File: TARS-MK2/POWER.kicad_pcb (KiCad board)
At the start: 2 copper layers, 69.9 x 162.4 mm, 20 parts, among them J701 XT60, J702 XT60, J703 SL_BATT1, J704 SL_BATT2, J705 TM_BATT1, J706 XT60, U701 D36V28F3, U702 D24V50F5, U703 LM7809_TO220, U704 D36V50F6, U705 D36V50F6, U706 D36V50F6, U707 D36V50F6

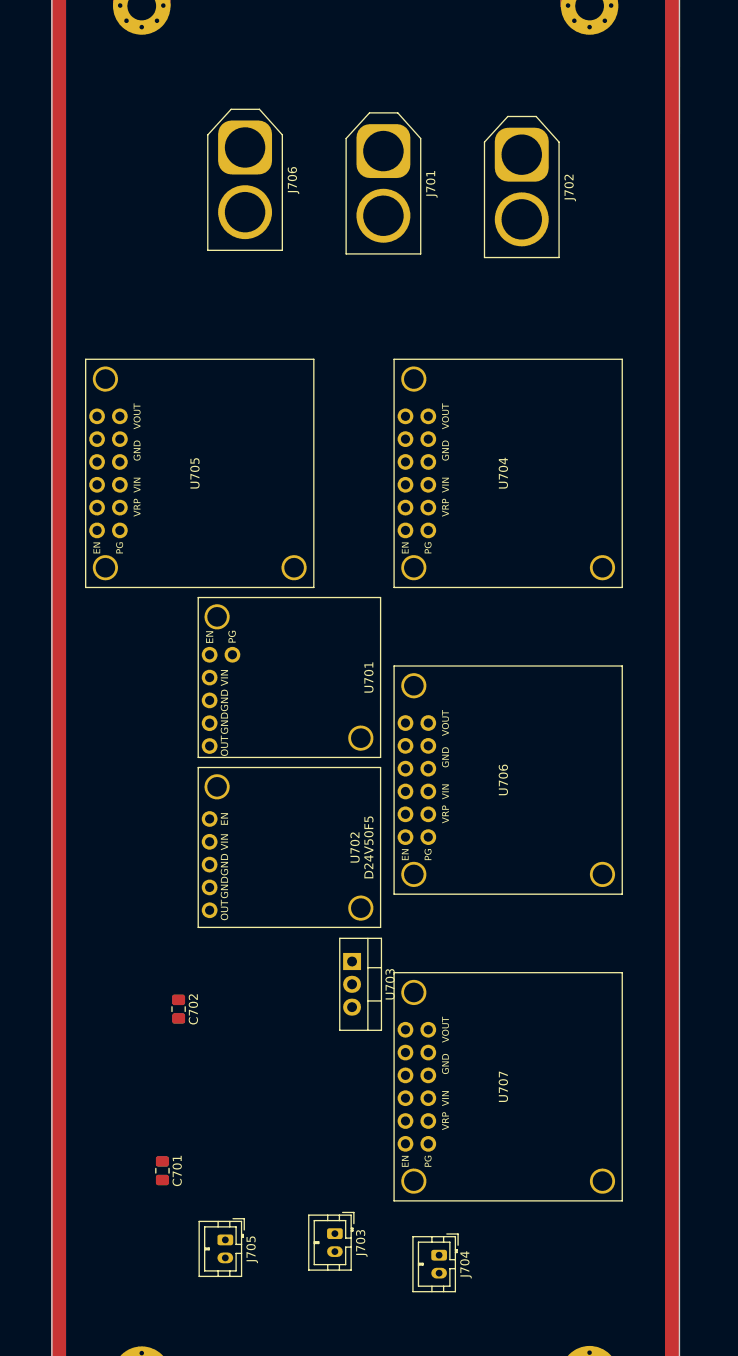
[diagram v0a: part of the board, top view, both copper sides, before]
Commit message: organized power board and added routes
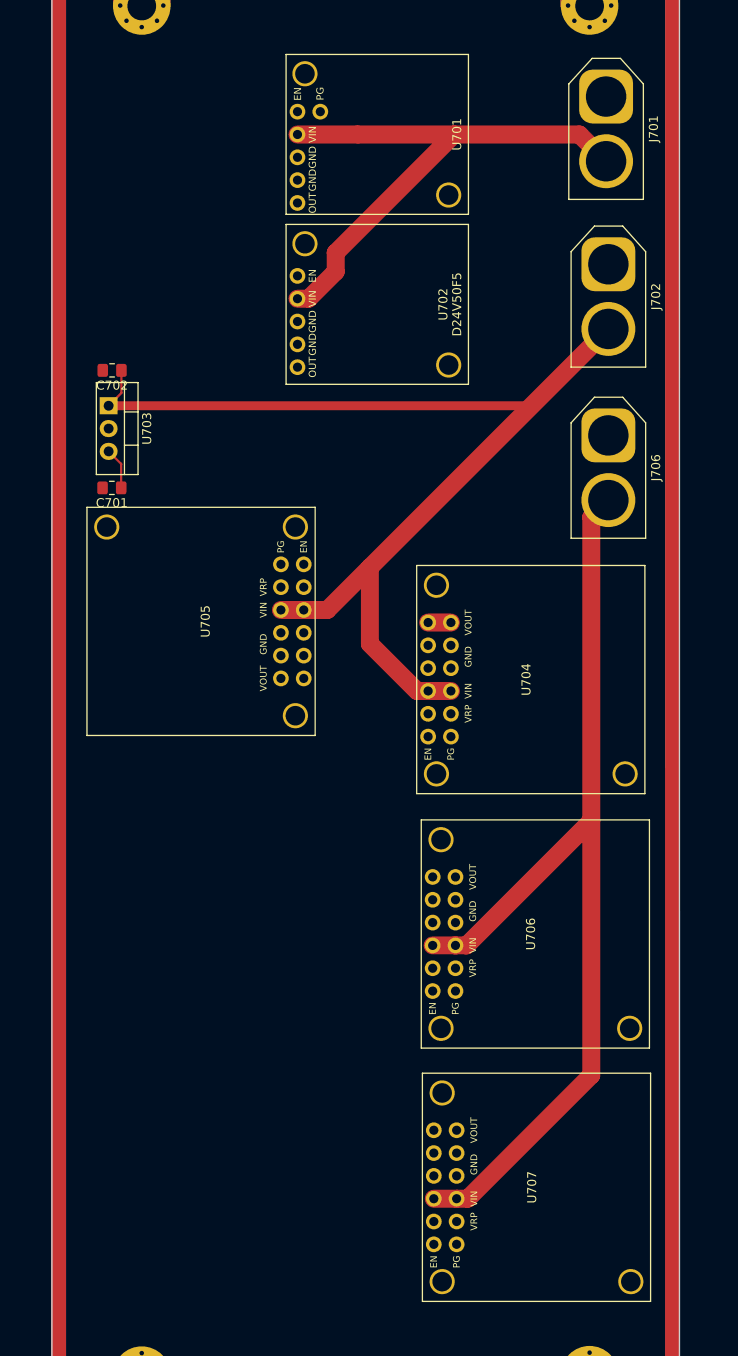
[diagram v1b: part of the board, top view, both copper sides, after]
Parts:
- removed J703: SL_BATT1, Connector_JST:JST_PH_B2B-PH-K_1x02_P2.00mm_Vertical
- removed J704: SL_BATT2, Connector_JST:JST_PH_B2B-PH-K_1x02_P2.00mm_Vertical
- removed J705: TM_BATT1, Connector_JST:JST_PH_B2B-PH-K_1x02_P2.00mm_Vertical
- moved C701 76.2 mm to (188.6, 118.5), turned to 180 degrees
- moved C702 71.5 mm to (188.6, 105.4), turned to 180 degrees
- moved U703 67.5 mm to (188.2, 109.3)
- moved U701 61.2 mm to (228.3, 79.1)
- moved U702 61.2 mm to (228.3, 98.1)
- moved J706 51.6 mm to (243.8, 112.6)
- moved U705 49.1 mm to (211.2, 146.1), turned to 90 degrees
- moved J701 25.5 mm to (243.6, 74.9)
- moved U704 23.1 mm to (222.5, 127.1)
- moved U706 17.4 mm to (223.0, 155.4)
- moved J702 15.5 mm to (243.8, 93.6)
- moved U707 11.6 mm to (223.1, 183.6)
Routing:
- net Net-(C702-Pad1): track 0.00 -> 133.3 mm
- net Net-(J706-Pad2): track 0.00 -> 111.4 mm
- net Net-(J701-Pad2): track 0.00 -> 61.8 mm
- net 9V_PT_SUPPLY: track 0.00 -> 4.64 mm
- net 6V_HYBRID_SERVO0: track 0.00 -> 2.54 mm

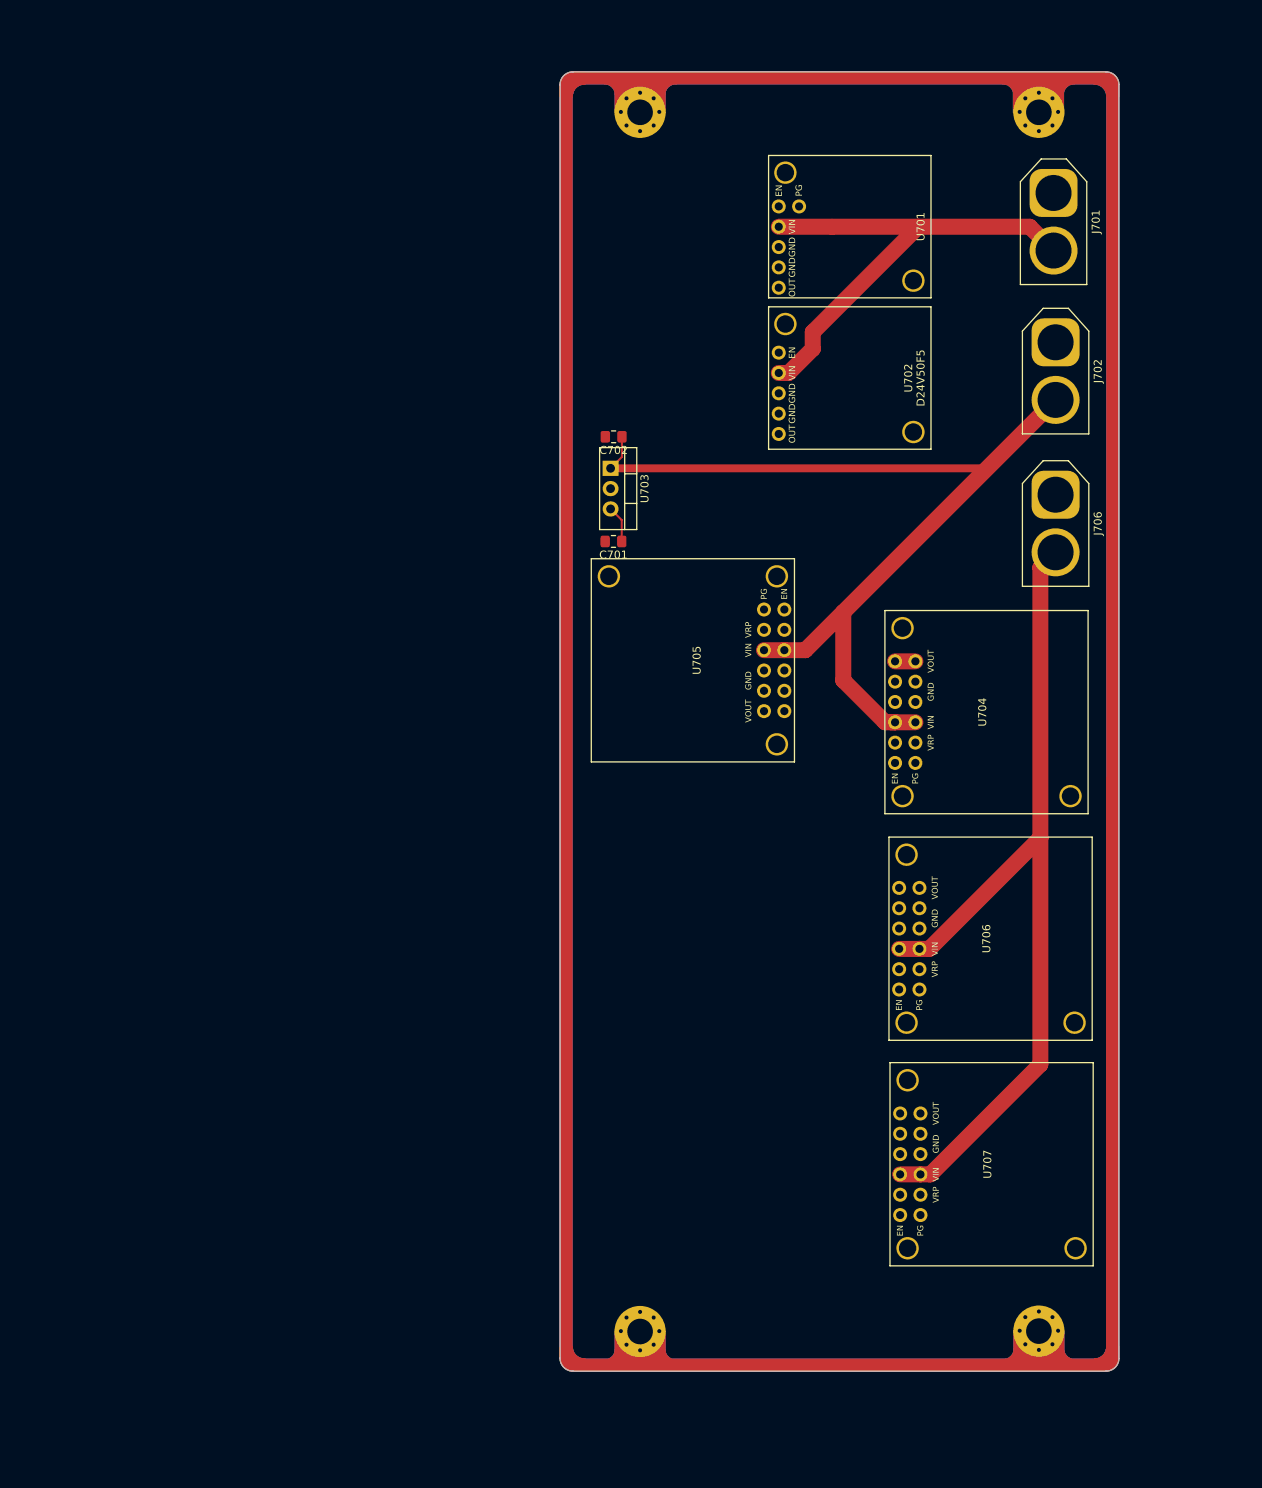
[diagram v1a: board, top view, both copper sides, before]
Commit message: Power Board molex connectors
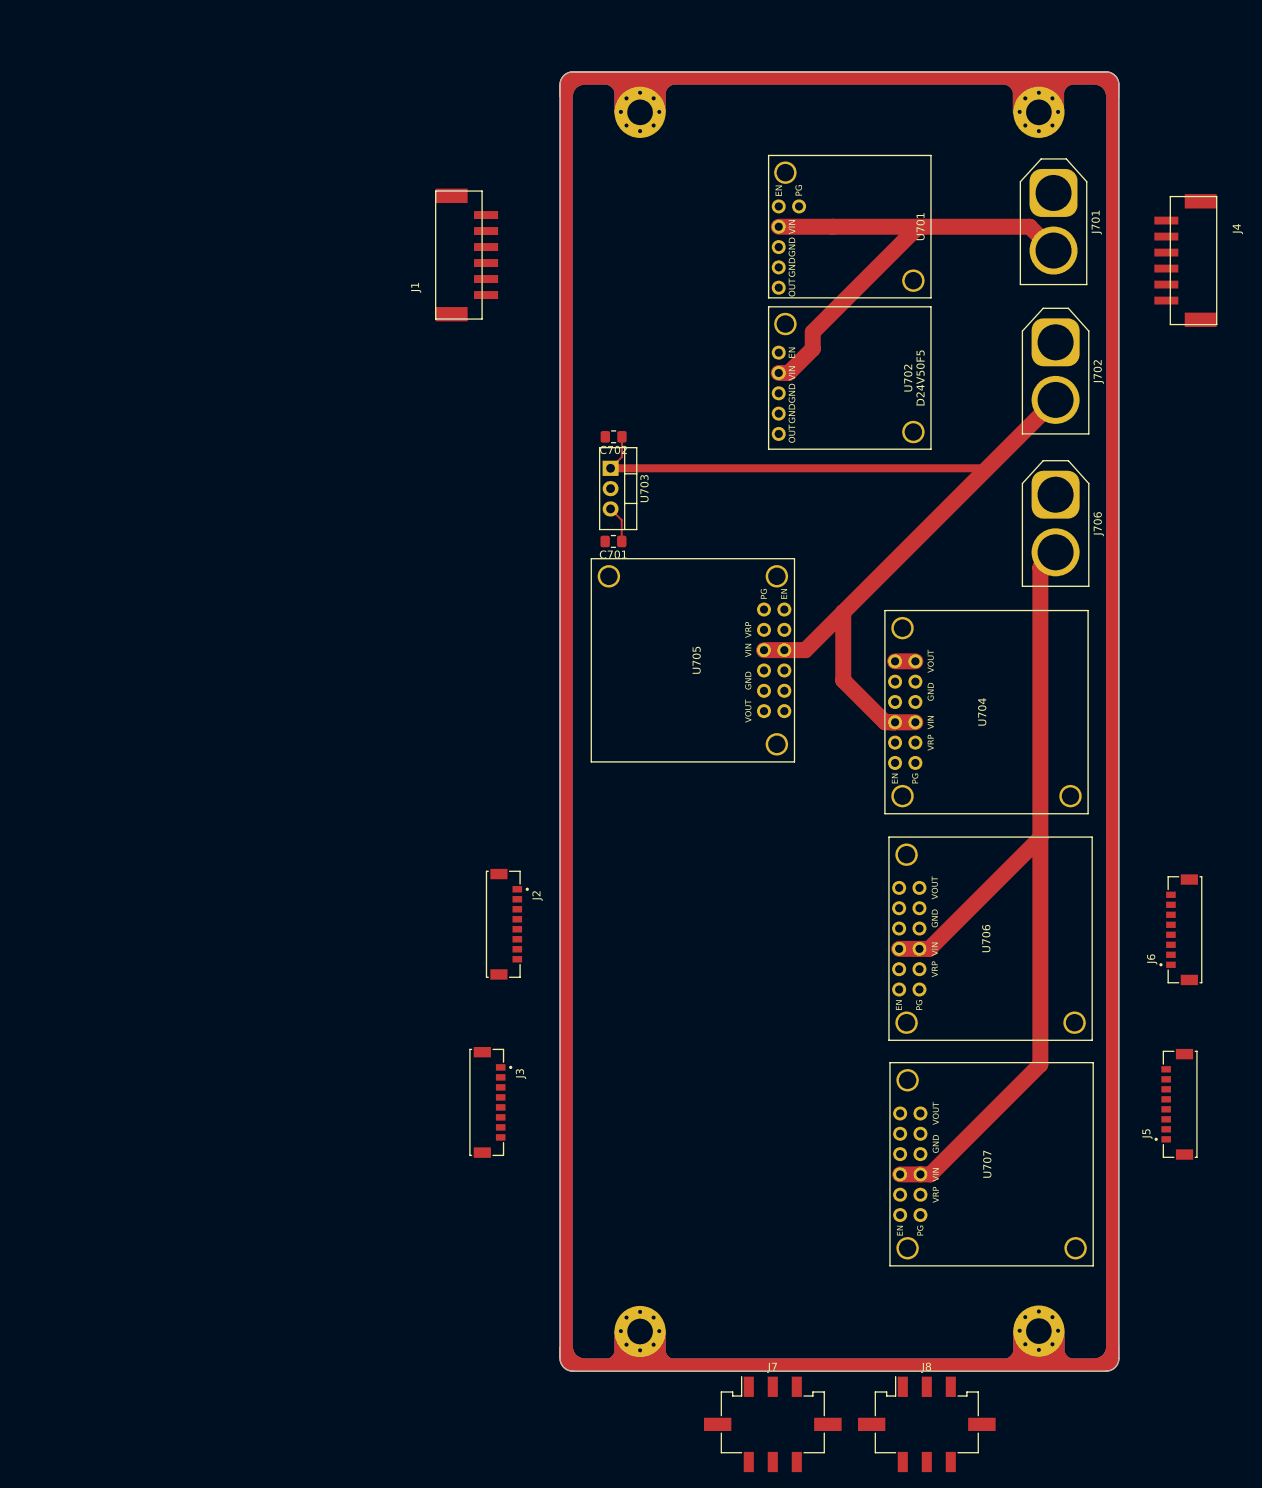
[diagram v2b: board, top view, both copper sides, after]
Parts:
- added J1: 505578-0671, Molex 6 Circuit 2.00mm:505578-0671, F.Cu at (166.3, 82.7)
- added J2: 505567-0871, Molex 8 Circuit 1.25mm:MOLEX_505567-0871, F.Cu at (174.8, 166.3)
- added J3: 505567-0871, Molex 8 Circuit 1.25mm:MOLEX_505567-0871, F.Cu at (172.7, 188.6)
- added J4: 505578-0671, Molex 6 Circuit 2.00mm:505578-0671, F.Cu at (264.0, 83.4)
- added J5: 505567-0871, Molex 8 Circuit 1.25mm:MOLEX_505567-0871, F.Cu at (259.4, 188.8)
- added J6: 505567-0871, Molex 8 Circuit 1.25mm:MOLEX_505567-0871, F.Cu at (260.0, 167.0)
- added J7: Conn_02x03_Top_Bottom_MountingPin, Connector_Molex:Molex_Micro-Fit_3.0_43045-0618_2x03-1MP_P3.00mm_Vertical, F.Cu at (208.5, 228.9)
- added J8: Conn_02x03_Top_Bottom_MountingPin, Connector_Molex:Molex_Micro-Fit_3.0_43045-0618_2x03-1MP_P3.00mm_Vertical, F.Cu at (227.7, 228.9)
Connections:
- net 6V_HYBRID_SERVO0 renamed 6V_HYBRID_SERVO3
- net 6V_HYBRID_SERVO1 renamed 6V_HYBRID_SERVO4
- U706 pad 12: 6V_AC_SERVO0 -> 6V_AC_SERVO1
- U706 pad 6: 6V_AC_SERVO0 -> 6V_AC_SERVO1
- U707 pad 12: 6V_AC_SERVO1 -> 6V_AC_SERVO2
- U707 pad 6: 6V_AC_SERVO1 -> 6V_AC_SERVO2

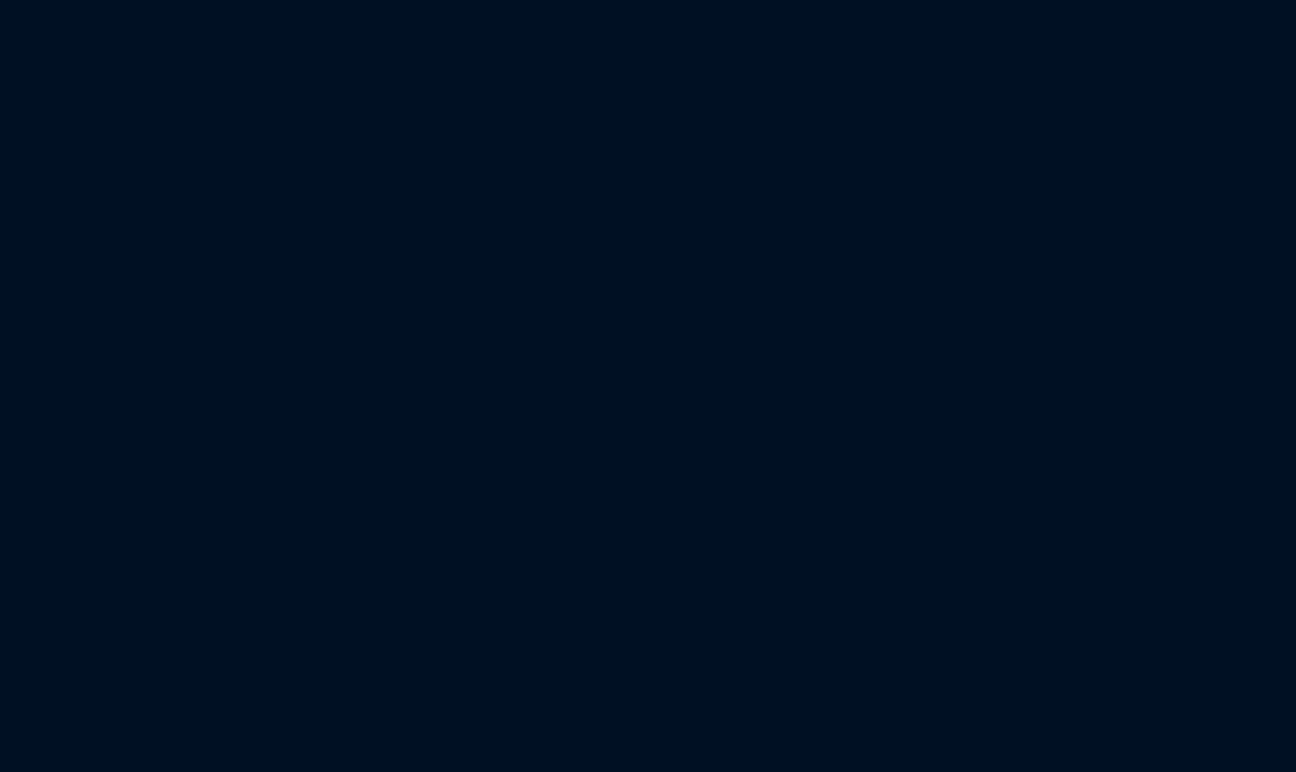
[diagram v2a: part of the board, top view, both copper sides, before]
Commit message: PT+SLND connections + various tweaks
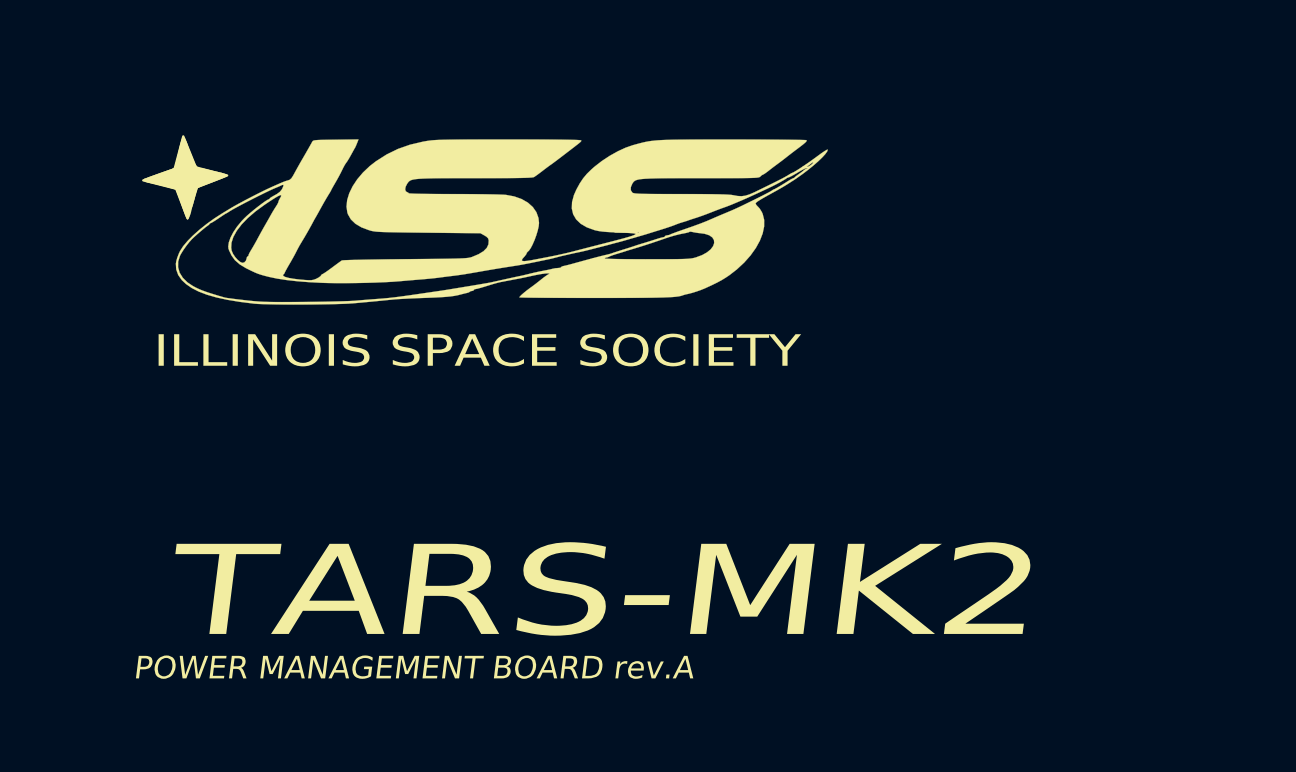
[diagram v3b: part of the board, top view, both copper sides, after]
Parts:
- added G***: LOGO, ISS_LOGO:ISS_LOGOV2_smaller, F.Cu at (133.8, 212.8)
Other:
- board text added: "POWER MANAGEMENT BOARD rev.A"
- board text added: "TARS-MK2"
